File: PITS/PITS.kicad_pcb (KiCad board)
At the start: 2 copper layers, 65 x 30 mm, 56 parts, among them P1 CONN_02X20, P10 I2C, P11 I2C, P12 I2C, P13 I2C, P14 BATT, P2 BNC, P3 BNC, P4 BNC, P5 BNC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

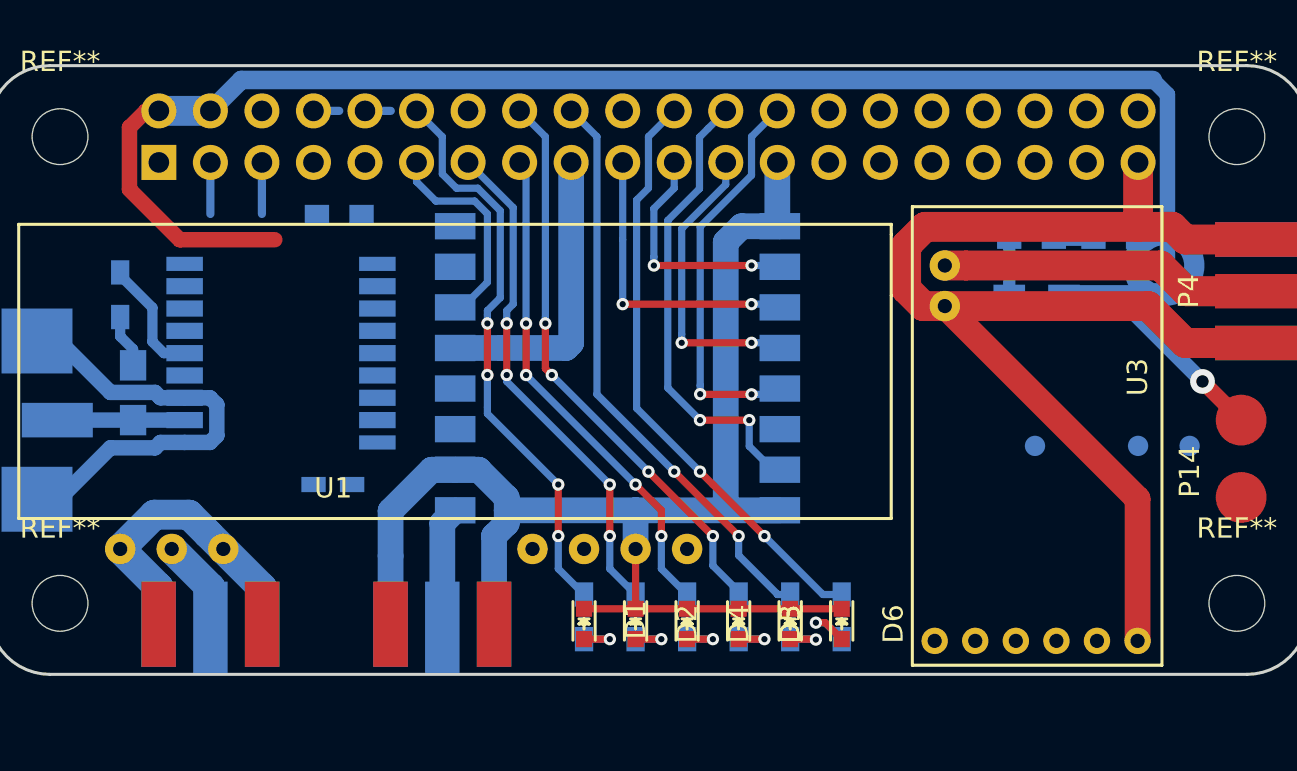
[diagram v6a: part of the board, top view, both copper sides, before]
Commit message: neue Pinbelegung
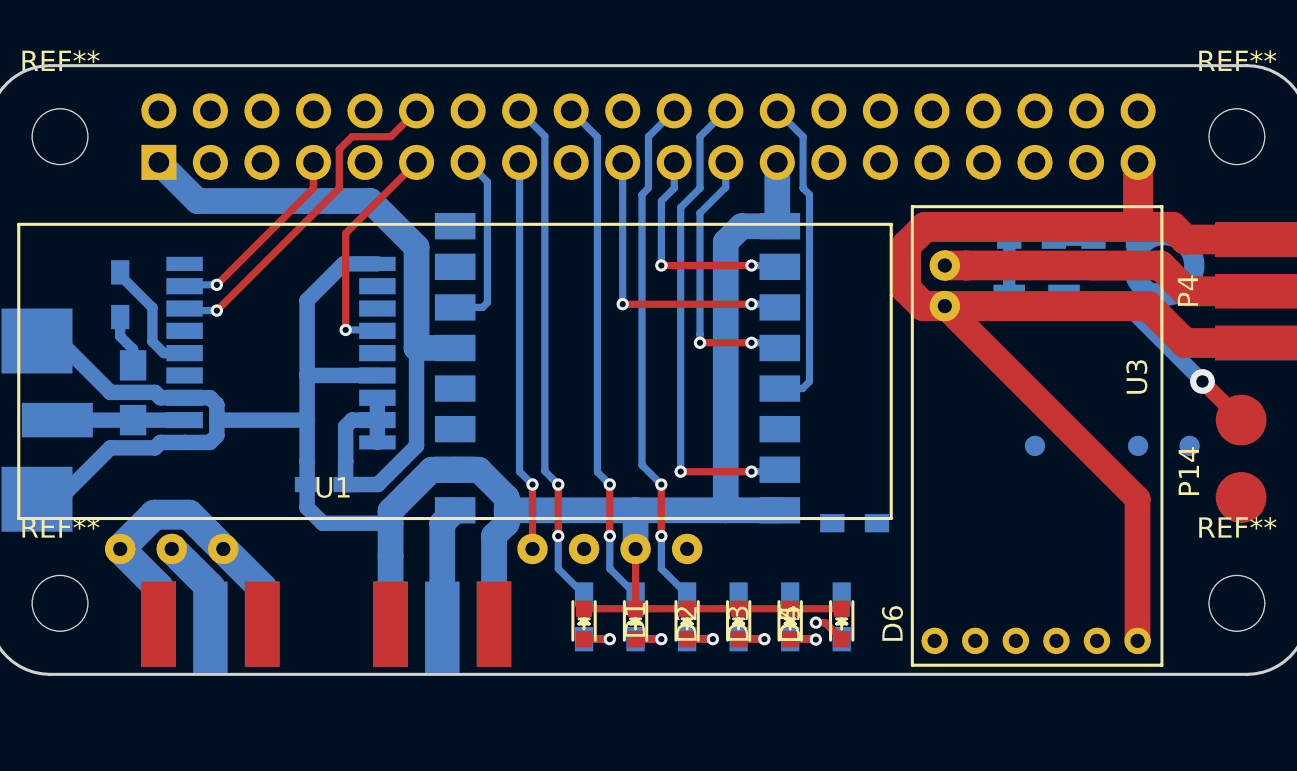
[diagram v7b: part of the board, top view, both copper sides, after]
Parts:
- moved R26 29.6 mm to (97.7, 71.5)
- moved D3 2.54 mm to (89.4, 76.5)
- moved D4 2.54 mm to (91.9, 76.5)
- moved R20 2.54 mm to (89.4, 76.2)
- moved R21 2.54 mm to (91.9, 76.2)
- moved C14 0.32 mm to (71.6, 69.6)
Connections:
- R14 pad 1: /GPIO18 -> /GPIO23
- R15 pad 1: /GPIO27 -> /GPIO24
- R20 pad 1: /GPIO23 -> /GPIO25
- R21 pad 1: /GPIO22 -> Net-(R21-Pad1)
- R22 pad 1: /GPIO24 -> Net-(R22-Pad1)
- R23 pad 1: /GPIO25 -> Net-(R23-Pad1)
- U1 pad 4: /GPIO25 -> /GPIO22
- U2 pad 16: /GPIO19(MISO1) -> /GPIO18
- U2 pad 17: /GPIO16(CE2) -> /GPIO4
- U2 pad 2: /GPIO15(RXD0) -> Net-(U2-Pad2)
- U2 pad 3: /GPIO14(TXD0) -> Net-(U2-Pad3)
- U2 pad 4: /GPIO12 -> /GPIO17
- U4 pad 14: /GPIO17 -> /GPIO27
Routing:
- net +5V: track 78.5 -> 0.00 mm
- net GND: track 171.0 -> 197.8 mm
- net +3V3: track 14.7 -> 37.4 mm
- net /GPIO27: track 25.0 -> 8.99 mm, vias 4 -> 0
- net /GPIO18: track 28.4 -> 16.7 mm, vias 4 -> 1
- net /GPIO4: track 0.00 -> 9.62 mm, vias 0 -> 1
- net /GPIO22: track 24.7 -> 19.3 mm, vias 4 -> 1
- net /GPIO7(CE1): track 19.6 -> 15.6 mm, vias 2 -> 0
- net /GPIO25: track 29.3 -> 25.4 mm
- net /GPIO24: track 28.7 -> 25.2 mm
- net /GPIO23: track 28.3 -> 25.2 mm, vias 4 -> 2
- net /GPIO3(SCL1): track 2.54 -> 0.00 mm
- net /GPIO2(SDA1): track 2.54 -> 0.00 mm
- net /GPIO11(SCLK0): track 14.7 -> 13.5 mm
- net /GPIO14(TXD0): track 1.27 -> 0.00 mm
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
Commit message: Layout - MTX2, HX1 and LEDs
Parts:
- removed R5: 10k, Resistors_SMD:R_0603_HandSoldering
- moved R4 68.1 mm to (103.5, 75.4), turned to 0 degrees
- moved R3 65.3 mm to (103.5, 73.5), turned to 0 degrees
- moved R2 61.9 mm to (108.3, 75.4), turned to 0 degrees
- moved R12 58.8 mm to (143.7, 55.9)
- moved R13 58.8 mm to (146.7, 54.8)
- moved R26 5.54 mm to (92.3, 72.8)
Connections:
- R21 pad 1: Net-(R21-Pad1) -> /GPIO12
- R22 pad 1: Net-(R22-Pad1) -> /GPIO5
- R23 pad 1: Net-(R23-Pad1) -> /GPIO6
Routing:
- net +3V3: track 37.4 -> 75.2 mm
- net /GPIO13: track 0.00 -> 32.4 mm, vias 0 -> 2
- net /GPIO12: track 0.00 -> 29.4 mm
- net /GPIO5: track 0.00 -> 23.1 mm
- net /GPIO6: track 0.00 -> 23.1 mm
- net /MTX2-TXD: track 0.00 -> 6.44 mm
- net GND: track 197.8 -> 201.4 mm
- net /HX1-TXD: track 0.00 -> 1.76 mm
